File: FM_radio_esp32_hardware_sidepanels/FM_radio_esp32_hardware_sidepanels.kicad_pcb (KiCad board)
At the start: 2 copper layers, 78 x 55 mm, 11 parts

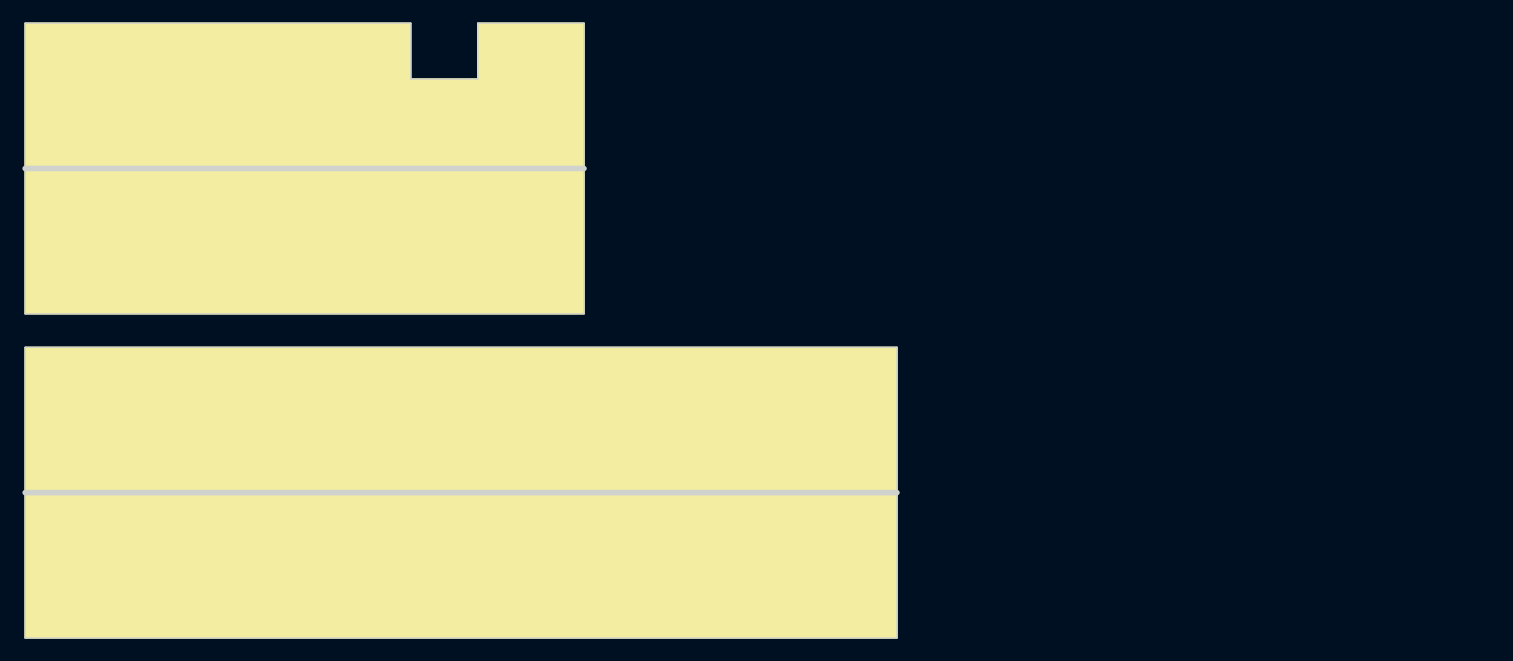
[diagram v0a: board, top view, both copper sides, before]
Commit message: new panelized data for side panels,
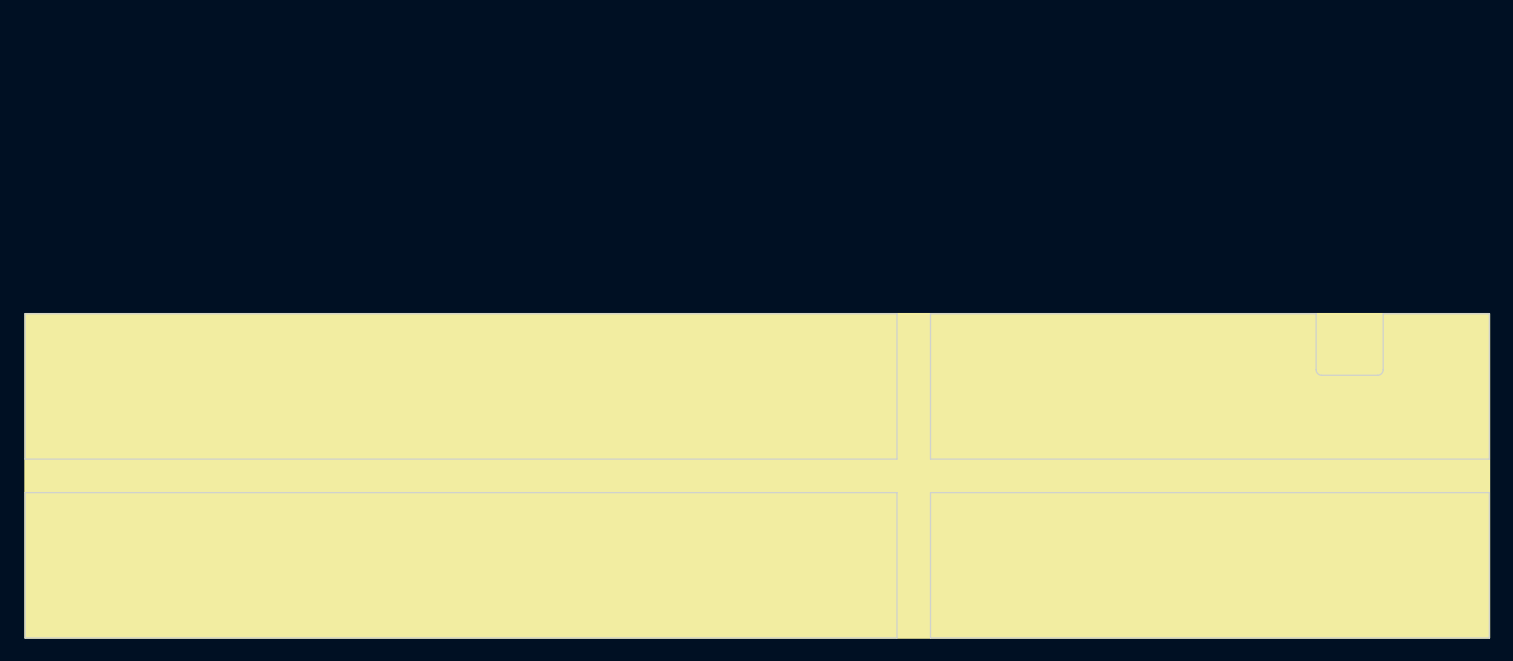
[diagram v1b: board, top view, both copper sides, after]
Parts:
- removed the G*** at (134.5, 103.0)
- added G***: LOGO, _local_Library:electronics_fig_4_long, B.Cu at (156.0, 115.5)
- moved H5 86.0 mm to (174.0, 123.5)
- moved H6 86.0 mm to (218.0, 123.5)
- moved H7 85.1 mm to (174.0, 107.5)
- moved H8 85.1 mm to (218.0, 107.5)
- moved H9 85.1 mm to (208.5, 110.5)
- moved TP1 85.1 mm to (198.0, 110.5)
- moved H3 3.00 mm to (93.0, 107.5)
- moved H4 3.00 mm to (165.0, 107.5)
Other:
- board size 78 x 55 mm -> 131 x 29 mm
